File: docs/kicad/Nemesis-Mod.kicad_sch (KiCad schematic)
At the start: 15 parts, among them M1 Pololu G2 HighPower 18v17, M1-M1 Pololu G2 HighPower 18v18, P1 Pololu_5V_Step_Down_Regulator, SW1 Reset, SW2 Rev SPDT Trigger, SW3 Firing SPDT Trigger

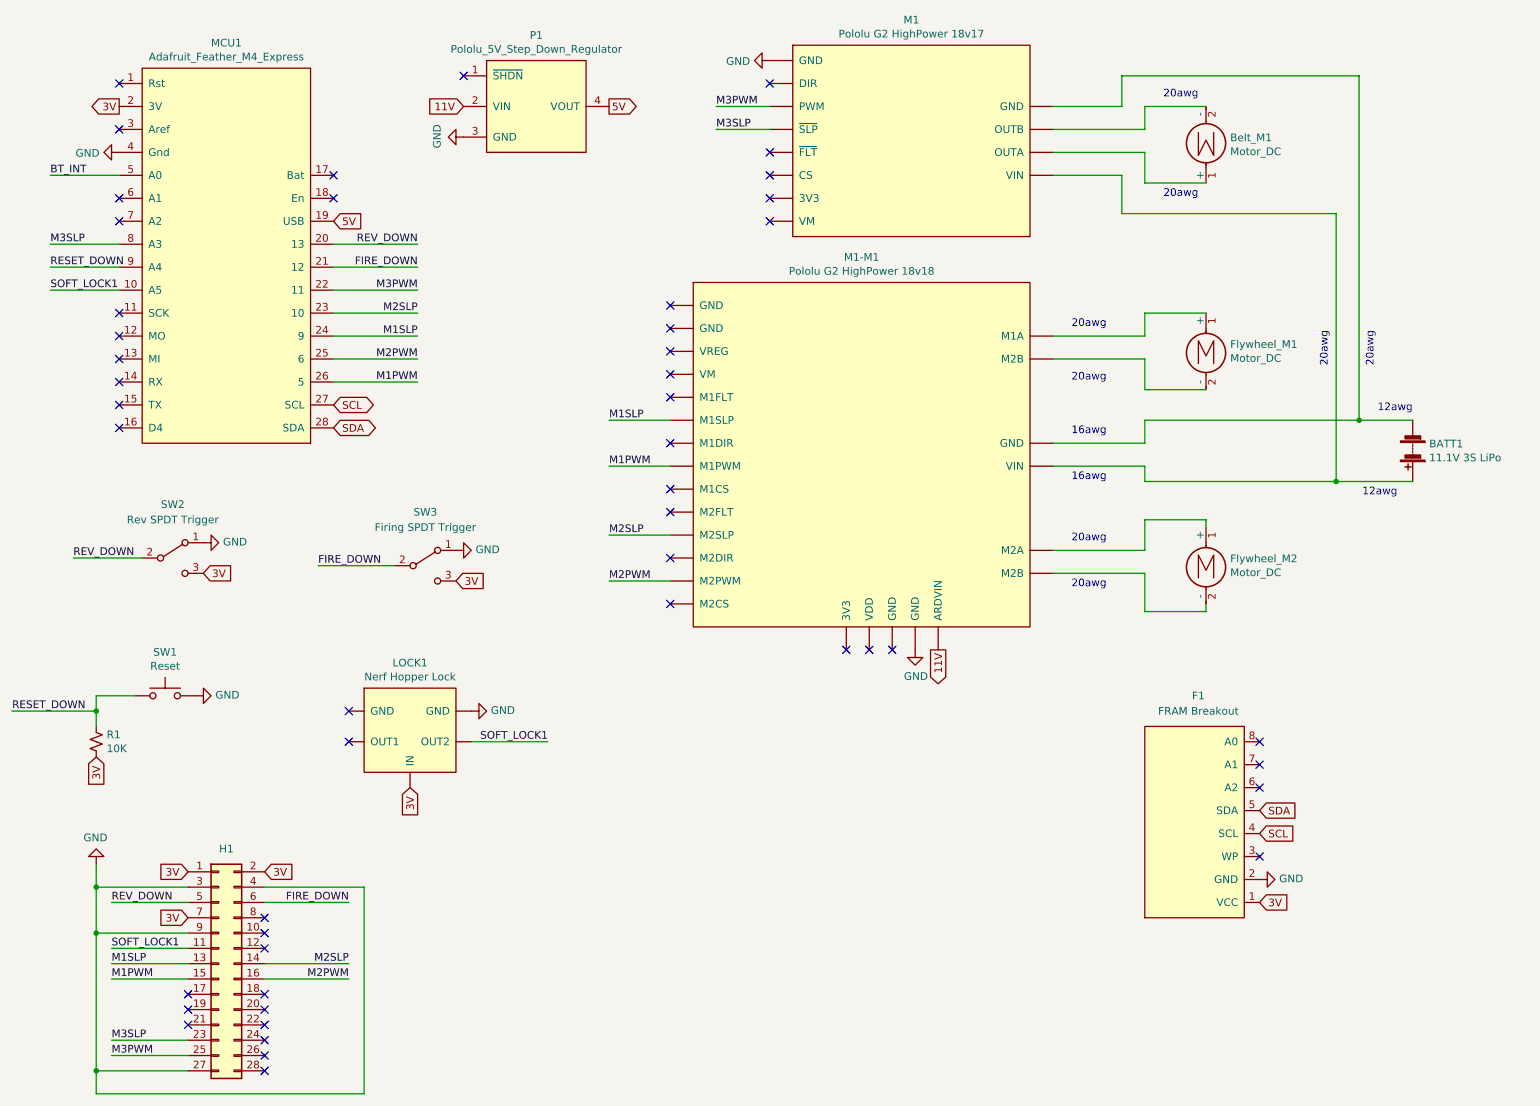
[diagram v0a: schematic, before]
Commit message: Reworking the schematic layout.
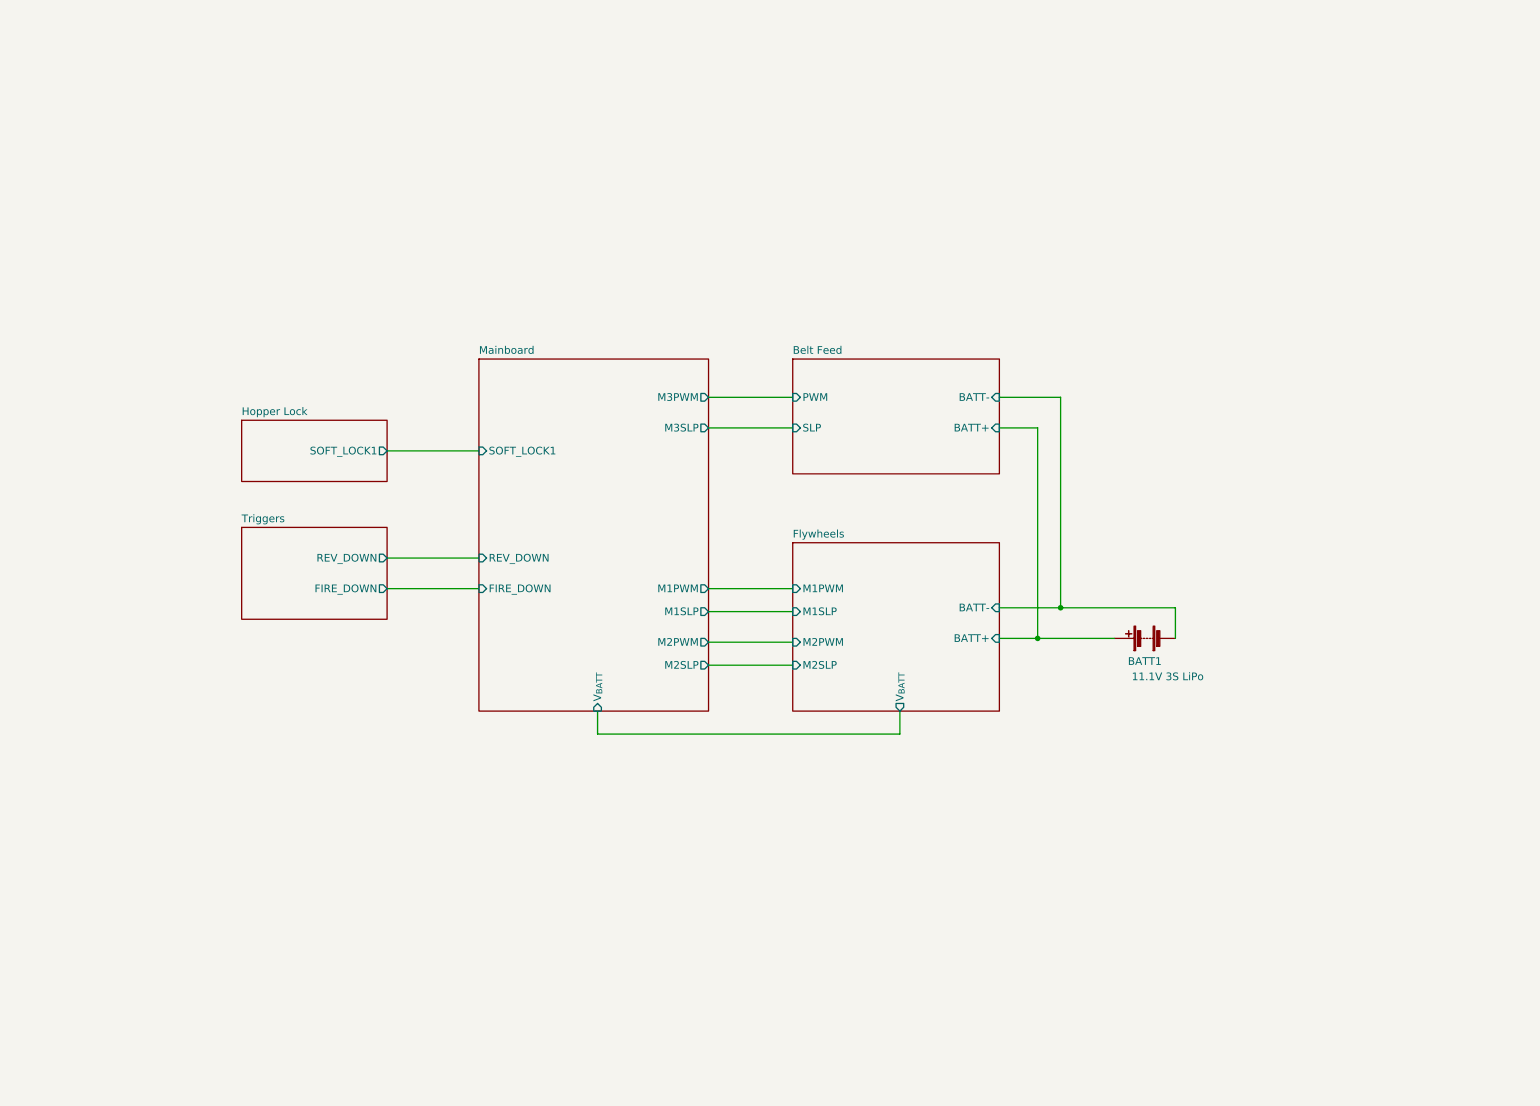
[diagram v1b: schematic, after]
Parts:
- removed BATT1: 11.1V 3S LiPo, symbol Device:Battery
- removed Belt_M1, Flywheel_M1, Flywheel_M2: Motor_DC, symbol Motor:Motor_DC
- removed F1: FRAM Breakout, Adafruit:Adafruit_I2C_FRAM_Breakout, symbol Nemesis-Mod:Adafruit_I2C_FRAM_Breakout
- removed H1: (no value), Connector_PinHeader_2.54mm:PinHeader_2x14_P2.54mm_Vertical, symbol Connector_Generic:Conn_02x14_Odd_Even
- removed LOCK1: Nerf Hopper Lock, symbol Nemesis-Mod:Nerf_Hopper_Lock
- removed M1: Pololu G2 HighPower 18v17, symbol Nemesis-Mod:Pololu_G2_HighPower_18v17
- removed M1-M1: Pololu G2 HighPower 18v18, symbol Nemesis-Mod:Pololu_G2_HighPower_18v18
- removed MCU1: Adafruit_Feather_M4_Express, Adafruit:Adafruit_Feather_M4_Express, symbol Nemesis-Mod:Adafruit_Feather_M4_Express
- removed P1: Pololu_5V_Step_Down_Regulator, Pololu:5V_Step_Down_Regulator_500mA, symbol Nemesis-Mod:Pololu_5V_Step_Down_Regulator
- removed R1: 10K, Resistor_THT:R_Axial_DIN0207_L6.3mm_D2.5mm_P5.08mm_Vertical, symbol Device:R_Small_US
- removed SW1: Reset, Button_Switch_THT:SW_PUSH_6mm, symbol Switch:SW_Push
- removed SW2: Rev SPDT Trigger, symbol Switch:SW_SPDT
- removed SW3: Firing SPDT Trigger, symbol Switch:SW_SPDT
- added BATT1: 11.1V 3S LiPo, symbol Nemesis-Mod:Battery
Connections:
- new net Belt Feed/BATT+: BATT1.1 (+)
- new net Belt Feed/BATT-: BATT1.2 (-)
- no-connect marks 49 -> 0
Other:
- added sheet Belt Feed (feed.kicad_sch)
- added sheet Flywheels (flywheels.kicad_sch)
- added sheet Hopper Lock (softlock.kicad_sch)
- added sheet Mainboard (main.kicad_sch)
- added sheet Triggers (triggers.kicad_sch)
- note removed: "12awg"
- note removed: "16awg"
- note removed: "20awg"
- company: https://github.com/jeff-winn/Nemesis-Mod -> https://github.com/jeff-winn/nemesis-mod
